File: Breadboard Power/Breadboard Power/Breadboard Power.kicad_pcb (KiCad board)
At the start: 2 copper layers, 69.8 x 42.9 mm, 32 parts, among them J1 Barrel_Jack, J2 Conn_02x05_Odd_Even, J3 Conn_02x05_Odd_Even, J4 Conn_02x08_Odd_Even, J5 Conn_02x08_Odd_Even, U1 LT1963, U2 LT3015

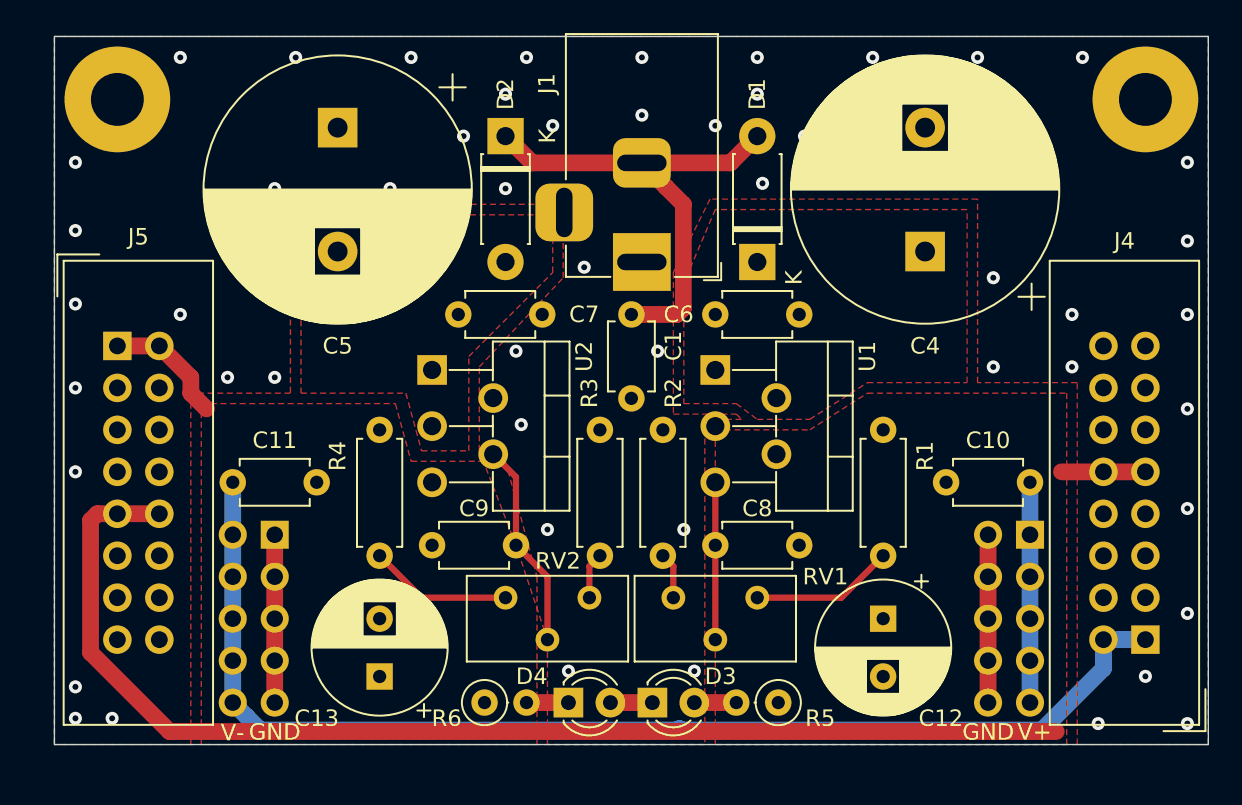
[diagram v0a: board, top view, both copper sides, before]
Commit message: updated breadboard power to REV 3
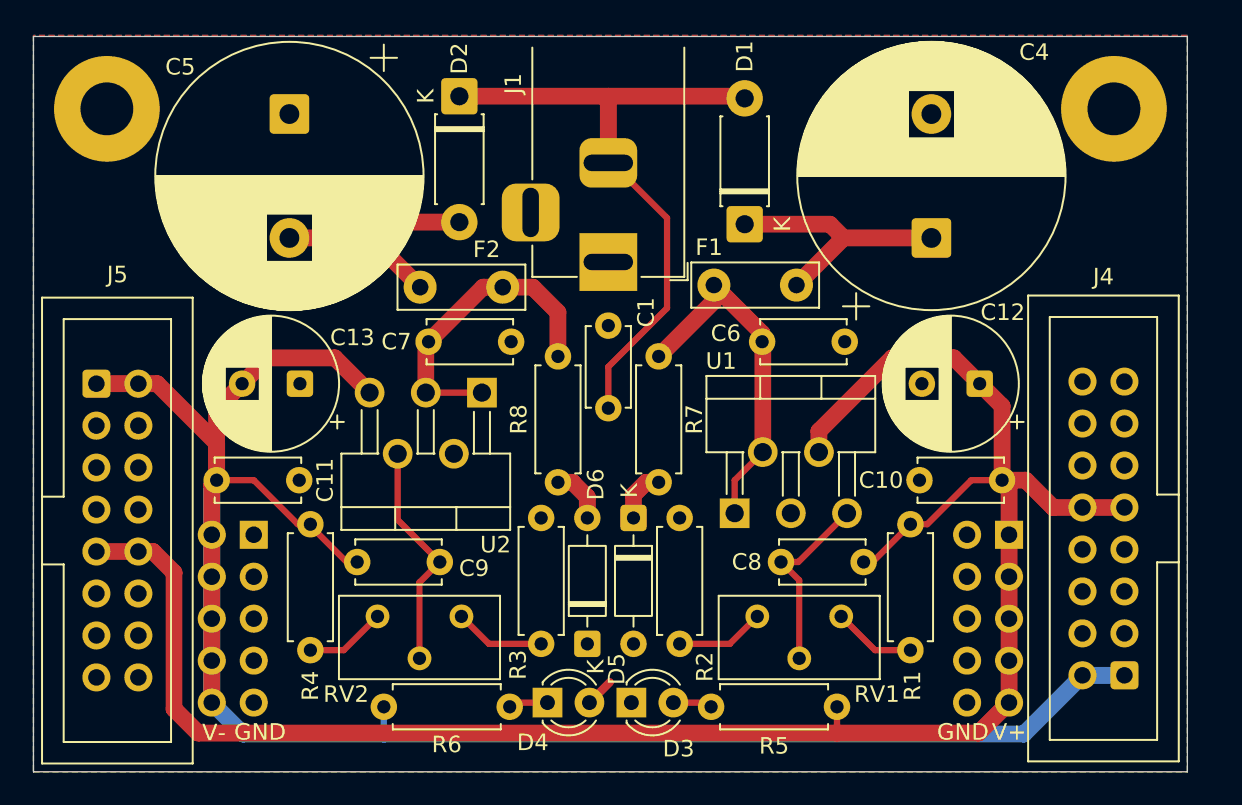
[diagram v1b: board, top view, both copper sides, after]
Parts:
- added D5: BZX55B18, Diode_THT:D_DO-35_SOD27_P7.62mm_Horizontal, F.Cu at (1.40, 9.14)
- added D6: BZX55B18, Diode_THT:D_DO-35_SOD27_P7.62mm_Horizontal, F.Cu at (-1.40, 16.8)
- added F1: BK60-030-DZ, Capacitor_THT:C_Disc_D7.5mm_W2.5mm_P5.00mm, F.Cu at (11.3, -4.95)
- added F2: BK60-030-DZ, Capacitor_THT:C_Disc_D7.5mm_W2.5mm_P5.00mm, F.Cu at (-11.5, -4.83)
- added R7: 100, Resistor_THT:R_Axial_DIN0207_L6.3mm_D2.5mm_P7.62mm_Horizontal, F.Cu at (2.92, -0.64)
- added R8: 100, Resistor_THT:R_Axial_DIN0207_L6.3mm_D2.5mm_P7.62mm_Horizontal, F.Cu at (-3.17, 6.99)
- C1: footprint NSI Footprints:C_Disc_D4mm_W2.6mm_P5.08mm -> Capacitor_THT:C_Disc_D4.7mm_W2.5mm_P5.00mm
- C10, C11, C6, C7, C8, C9: footprint NSI Footprints:C_Disc_D4mm_W2.6mm_P5.08mm -> Capacitor_THT:C_Disc_D5.0mm_W2.5mm_P5.00mm
- R1: value 150k -> 47k
- R2, R3: value 13k -> 5.1k
- R4: value 160k -> 47k
- R5: value 5.1k -> 620k; footprint Resistor_THT:R_Axial_DIN0207_L6.3mm_D2.5mm_P2.54mm_Vertical -> Resistor_THT:R_Axial_DIN0207_L6.3mm_D2.5mm_P7.62mm_Horizontal
- R6: value 4.7k -> 750k; footprint Resistor_THT:R_Axial_DIN0207_L6.3mm_D2.5mm_P2.54mm_Vertical -> Resistor_THT:R_Axial_DIN0207_L6.3mm_D2.5mm_P7.62mm_Horizontal
- RV1, RV2: value 20k -> 500; footprint NSI Footprints:Potentiometer_TT_67Y_Vertical -> Potentiometer_THT:Potentiometer_Bourns_3296Y_Vertical
- moved C13 18.4 mm to (-18.8, 1.02), turned to 180 degrees
- moved C12 15.4 mm to (22.4, 1.02), turned to 180 degrees
- moved U1 8.75 mm to (7.52, 8.86), turned to 0 degrees
- moved RV2 7.83 mm to (-9.02, 15.1)
- moved R4 7.09 mm to (-18.2, 17.1)
- moved R3 6.41 mm to (-4.19, 9.14)
- moved R6 6.10 mm to (-13.7, 20.6)
- moved R1 5.95 mm to (18.2, 9.53)
- moved R2 5.43 mm to (4.19, 16.8)
- moved RV1 5.20 mm to (14.0, 15.1)
- moved C9 4.72 mm to (-10.3, 11.8)
- moved C1 4.62 mm to (-0.13, -2.50), turned to -90 degrees
- moved C8 4.03 mm to (15.3, 11.8)
- moved D2 3.69 mm to (-9.14, -16.4)
- moved R5 3.57 mm to (13.7, 20.6)
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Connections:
- C4 pad 1: Net-(C4-Pad1) -> Net-(D1-K)
- C5 pad 2: Net-(C5-Pad2) -> Net-(D2-A)
- C6 pad 1: Net-(C4-Pad1) -> Net-(U1-IN)
- C7 pad 2: Net-(C5-Pad2) -> Net-(U2-IN)
- D1 pad 1: Net-(C4-Pad1) -> Net-(D1-K)
- D2 pad 2: Net-(C5-Pad2) -> Net-(D2-A)
- U1 pad 1: Net-(C4-Pad1) -> Net-(U1-IN)
- U1 pad 2: Net-(C4-Pad1) -> Net-(U1-IN)
- U2 pad 1: Net-(C5-Pad2) -> Net-(U2-IN)
- U2 pad 3: Net-(C5-Pad2) -> Net-(U2-IN)
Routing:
- net VEE: track 80.2 -> 123.5 mm
- net VCC: track 91.2 -> 119.0 mm
- net Net-(U1-IN): track 0.00 -> 21.4 mm
- net GND: track 22.9 -> 1.74 mm, vias 55 -> 0
- net Net-(U2-IN): track 0.00 -> 19.1 mm
- net Net-(D1-K): track 0.00 -> 15.7 mm
- net Net-(D2-A): track 0.00 -> 14.9 mm
- net Net-(D1-A): track 29.7 -> 39.3 mm
- net Net-(R4-Pad1): track 8.67 -> 4.91 mm
- net Net-(R1-Pad2): track 8.67 -> 5.04 mm
- net Net-(D6-A): track 0.00 -> 3.42 mm
- net Net-(D5-K): track 0.00 -> 3.24 mm
- net Net-(R3-Pad2): track 2.80 -> 5.51 mm
- net Net-(R2-Pad1): track 2.80 -> 5.39 mm
- net Net-(U1-ADJ): track 9.53 -> 11.5 mm
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- removed copper zone on F.Cu, net Net-(C4-Pad1)
- removed copper zone on F.Cu, net Net-(C5-Pad2)
- removed copper zone on F.Cu, net VCC
- removed copper zone on F.Cu, net VEE
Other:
- board size 69.8 x 42.9 mm -> 69.8 x 44.5 mm
- board text added: "BREADBOARD POWER REV 3"
- board text removed: "BREADBOARD POWER REV 2"
